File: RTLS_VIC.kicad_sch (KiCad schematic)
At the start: 35 parts, among them J1 Conn_01x02_Pin, SW1 TS-1187A-B-A-B, U1 STM32WLE5CBUx, U3 HXY4612S, U4 TPS63900DSKR, X1 Q24FA20H0021700

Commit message: add notes
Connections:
- net +BATT: no longer C21.1, U4.1 (EN), U4.10 (VIN)
- new net +ESC_5V: C21.1, U4.1 (EN), U4.10 (VIN)
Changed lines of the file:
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@@
 			)
 		)
-		(property "Value" "+BATT"
-			(at 184.15 134.6199 90)
+		(property "Value" "+ESC_5V"
+			(at 186.69 132.08 90)
 			(effects
 				(font
 					(size 1.27 1.27)
 				)
-				(justify left)
 			)
 		)

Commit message: major overhaul
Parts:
- removed C20, C5: 10nF, Capacitor_SMD:C_0402_1005Metric, symbol Device:C
- removed C21, C22, C23: 10uF, Capacitor_SMD:C_0402_1005Metric, symbol Device:C
- removed C25, C26: 12pF, Capacitor_SMD:C_0402_1005Metric, symbol Device:C
- removed C4: 1uF, Capacitor_SMD:C_0402_1005Metric, symbol Device:C
- removed C6, C7, C8: 100nF, Capacitor_SMD:C_0402_1005Metric, symbol Device:C
- removed J1: Conn_01x02_Pin, Connector_PinHeader_2.54mm:PinHeader_1x02_P2.54mm_Vertical, symbol Connector:Conn_01x02_Pin
- removed L6: DFE201612E-2R2M=P2, dfe2016:L0806, symbol dfe2016:DFE201612E-2R2M=P2
- removed R6: 24k, Resistor_SMD:R_0603_1608Metric, symbol Device:R
- removed R7: 100k, Resistor_SMD:R_0603_1608Metric, symbol Device:R
- removed R8: 36k5, Resistor_SMD:R_0603_1608Metric, symbol Device:R
- removed SW1: TS-1187A-B-A-B, ts-1187a-b-a-b:SW-SMD_4P-L5.1-W5.1-P3.70-LS6.5-TL_H1.5, symbol ts-1187a-b-a-b:TS-1187A-B-A-B
- removed U1: STM32WLE5CBUx, Package_DFN_QFN:QFN-48-1EP_7x7mm_P0.5mm_EP5.6x5.6mm, symbol MCU_ST_STM32WL:STM32WLE5CBUx
- removed U3: HXY4612S, hxy4612s:SOP-8_L4.9-W3.9-P1.27-LS6.0-BL, symbol hxy4612s:HXY4612S
- removed U4: TPS63900DSKR, tps63900:WSON-10_L2.5-W2.5-W0.50-TL-EP, symbol tps63900:TPS63900DSKR
- removed X1: Q24FA20H0021700, q24:CRYSTAL-SMD_4P-L2.5-W2.0-BL, symbol q24:Q24FA20H0021700
- added C10, C11: 18pF, Capacitor_SMD:C_0402_1005Metric, symbol Device:C
- added C12, C13, C14, C15, C16, C9: 100nF, Capacitor_SMD:C_0402_1005Metric, symbol Device:C
- added C17: 1uF, Capacitor_SMD:C_0402_1005Metric, symbol Device:C
- added D2, D3: LED, LED_SMD:LED_0603_1608Metric, symbol Device:LED
- added J8: Conn_01x02_Pin, Connector_PinHeader_2.54mm:PinHeader_1x02_P2.54mm_Vertical, symbol Connector:Conn_01x02_Pin
- added L1: DFE201612E-2R2M=P2, lib:L0806, symbol lib:DFE201612E-2R2M=P2
- added R2: 10K, Resistor_SMD:R_0603_1608Metric, symbol Device:R
- added SW1: TS-1187A-B-A-B, lib:SW-SMD_4P-L5.1-W5.1-P3.70-LS6.5-TL_H1.5, symbol lib:TS-1187A-B-A-B
- added U2: TPS63900DSKR, lib:WSON-10_L2.5-W2.5-W0.50-TL-EP, symbol lib:TPS63900DSKR
- added U9: STM32F411RET6, lib:LQFP-64_L10.0-W10.0-P0.50-LS12.0-BL, symbol lib:STM32F411RET6
- added X1: XL2EL89COI-111YLC-26M, lib:CRYSTAL-SMD_4P-L3.2-W2.5-BL_SIT8008BI, symbol lib:XL2EL89COI-111YLC-26M
- C1, C2: value 100nF -> 10uF; LCSC (none) -> C15525
- C3: value 4.7uF -> 10uF; LCSC (none) -> C15525
- R1: value 10K -> 100k; LCSC (none) -> C25803
- R3: value 100K -> 36k5; LCSC (none) -> C23029
- R4: value 7k5 -> 1K
- R5: value 100K -> 1K
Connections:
- net MEAS_EN is gone; now on net GND: R3.1
- net +3V3: now also C12.1, C13.1, C14.1, C15.1, C16.1, C17.1, J8.2 (Pin_2), U2.6 (VOUT), U9.1 (VBAT), U9.19 (VDD), U9.32 (VDD), U9.48 (VDD), U9.64 (VDD); no longer C1.1
- net +ESC_5V: now also C1.1, U2.1 (EN), U2.10 (VIN)
- net GND: now also R1.1, C10.2, C11.1, C12.2, C13.2, C14.2, C15.2, C16.2, C17.2, C9.1, D2.1 (K), D3.1 (K), R2.2, SW1.1 (A), SW1.2 (B), U2.5 (CFG3), U2.8 (GND), U9.12 (VSSA/VREF-), U9.18 (VSS), U9.31 (VSS), U9.47 (VSS), U9.63 (VSS), X1.2 (GND), X1.4 (GND); no longer R1.2, R3.2
- net GPS_RX: now also U9.17 (PA3)
- net GPS_TX: now also U9.16 (PA2)
- net NSS: now also U9.20 (PA4)
- net PWM_1: now also U9.44 (PA11)
- net PWM_2: now also U9.43 (PA10)
- net PWM_3: now also U9.42 (PA9)
- net PWM_4: now also U9.41 (PA8)
- net PWR_SEL: now also R1.2, U2.2 (SEL), U9.33 (PB12)
- net RST: now also C9.2, SW1.3 (C), SW1.4 (D), U9.7 (NRST)
- net SCL: now also U9.58 (PB6)
- net SDA: now also U9.59 (PB7)
- net LED_DEBUG_3: now reaches R4.2
- net LED_DEBUG_3: now also U9.36 (PB15)
- net at R5.1: now also D3.2 (A)
- net +3.3VA renamed VDDA
- net VDDA: now also U9.13 (VDDA/VREF+)
- net +BATT renamed LED_DEBUG_2
- net LED_DEBUG_2: now also U9.35 (PB14)
- net DEBUG_SWCLK renamed SWCLK
- net SWCLK: now also U9.49 (PA14)
- net DEBUG_SWDIO renamed SWDIO
- net SWDIO: now also U9.46 (PA13)
- net LED_DEBUG renamed LED_DEBUG_1
- net LED_DEBUG_1: now also U9.34 (PB13)
- net MEAS_OUT: no longer names the net of R4.1
- net MEAS_OUT: now also D2.2 (A)
- net RX renamed DEBUG_RX
- net DEBUG_RX: now also U9.55 (PB3)
- net TX renamed DEBUG_TX
- net DEBUG_TX: now also U9.50 (PA15)
- new net: R3.2, U2.3 (CFG1)
- new net: L1.2, U2.7 (LX2)
- new net: L1.1, U2.9 (LX1)
- new net BOOT0: J8.1 (Pin_1), R2.1, U9.60 (BOOT0)
- new net SPI_MISO: U9.22 (PA6)
- new net SPI_MOSI: U9.23 (PA7)
- new net SPI_SCK: U9.21 (PA5)
- new net XIN: C11.2, U9.5 (PH0_OSC_IN), X1.1
- new net XOT: C10.1, U9.6 (PH1_OSC_OUT), X1.3
- no-connect marks 10 -> 6
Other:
- removed sheet Radio + Antenna
- moved on the sheet: C24, D1, J2, L7, R10, R11, R9

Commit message: working on placements
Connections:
- net DEBUG_BTN_1: now reaches U9.39 (PC8)
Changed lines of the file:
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@@
+		)
+	)
+	(global_label "DEBUG_BTN_1"
+		(shape input)
+		(at 106.68 95.25 0)
+		(fields_autoplaced yes)
+		(effects
+			(font
+				(size 1.27 1.27)
+			)
+			(justify left)
+		)
+		(property "Intersheetrefs" "${INTERSHEET_REFS}"
+			(at 122.6675 95.25 0)
+			(effects
+				(font
+					(size 1.27 1.27)
+				)
+				(justify left)
+				(hide yes)
+			)
 		)
 	)

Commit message: nearly there
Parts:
- added C4: 4.7uF, Capacitor_SMD:C_0402_1005Metric, symbol Device:C
- added J10, J11, J13: Conn_01x04_Socket, Connector_PinSocket_2.54mm:PinSocket_1x04_P2.54mm_Vertical, symbol Connector:Conn_01x04_Socket
- added J12: Conn_01x02_Pin, Connector_PinHeader_2.54mm:PinHeader_1x02_P2.54mm_Vertical, symbol Connector:Conn_01x02_Pin
- J8: now left out of the parts list
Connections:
- net +3V3: now also J10.1 (Pin_1), J12.2 (Pin_2), J13.1 (Pin_1)
- net GND: now also C4.2, J10.4 (Pin_4), J12.1 (Pin_1), J13.4 (Pin_4)
- net SCL: now also J10.3 (Pin_3)
- net SDA: now also J10.2 (Pin_2)
- net SPI_MISO: now also J11.3 (Pin_3)
- net SPI_MOSI: now also J11.4 (Pin_4)
- net SPI_SCK: now also J11.2 (Pin_2)
- net BMP581_INT: now reaches U9.27 (PB1)
- net LSM6_INT1: now reaches U9.28 (PB2)
- net LSM6_INT2: now reaches U9.29 (PB10)
- net VCAP: now reaches U9.30 (VCAP_1)
- net VCAP: now also C4.1
- net DEBUG_UART6_TX: now reaches U9.37 (PC6)
- net DEBUG_UART6_TX: now also J13.2 (Pin_2)
- net DEBUG_UART6_RX: now reaches U9.38 (PC7)
- net DEBUG_UART6_RX: now also J13.3 (Pin_3)
- net DEBUG_NSS: now reaches U9.45 (PA12)
- net DEBUG_NSS: now also J11.1 (Pin_1)
- no-connect marks 6 -> 23
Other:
- sheet Sensors ports: added BMP581_INT, LSM6_INT1, LSM6_INT2; removed none
- note added: "TODO: Look at the .ioc and include the timing channels for backup PWM channels break out timing channels 2 to pins behind the existing pwm out"
- note added: "Test Connectors"
- moved on the sheet: C1, C2, C3, L1, R1, R3, U2

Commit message: preparing for prod
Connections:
- net DEBUG_NSS: now also U9.24 (PC4); no longer U9.45 (PA12)
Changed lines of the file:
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@@
+	)
+	(no_connect
+		(at 106.68 80.01)
 	)
 	(no_connect
@@
 	(no_connect
 		(at 262.89 36.83)
-	)
-	(no_connect
-		(at 66.04 130.81)
 	)
 	(wire
@@
 		)
 	)
+	(global_label "DEBUG_NSS"
+		(shape input)
+		(at 66.04 130.81 270)
+		(fields_autoplaced yes)
+		(effects
+			(font
+				(size 1.27 1.27)
+			)
+			(justify right)
+		)
+		(property "Intersheetrefs" "${INTERSHEET_REFS}"
+			(at 66.04 144.8018 90)
+			(effects
+				(font
+					(size 1.27 1.27)
+				)
+				(justify right)
+				(hide yes)
+			)
+		)
+	)
 	(global_label "LSM6_INT1"
 		(shape output)
@@
 				(hide yes)
 			)
-		)
-	)
-	(global_label "DEBUG_NSS"
-		(shape input)
-		(at 106.68 80.01 0)
-		(fields_autoplaced yes)
-		(effects
-			(font
-				(size 1.27 1.27)
-			)
-			(justify left)
-		)
-		(property "Intersheetrefs" "${INTERSHEET_REFS}"
-			(at 120.6718 80.01 0)
-			(effects
-				(font
-					(size 1.27 1.27)
-				)
-				(justify left)
-				(hide yes)
-			)

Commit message: prod1
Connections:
- net BMP581_INT: no longer names the net of U9.27 (PB1)
- no-connect marks 23 -> 24
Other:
- sheet Sensors ports: added none; removed BMP581_INT
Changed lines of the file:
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@@
 	)
 	(no_connect
+		(at 73.66 130.81)
+	)
+	(no_connect
 		(at 73.66 52.07)
 	)
@@
 		)
 	)
-	(global_label "BMP581_INT"
-		(shape output)
-		(at 73.66 130.81 270)
-		(effects
-			(font
-				(size 1.27 1.27)
-			)
-			(justify right)
-		)
-		(property "Intersheetrefs" "${INTERSHEET_REFS}"
-			(at 73.66 130.81 0)
-			(effects
-				(font
-					(size 1.27 1.27)
-				)
-				(hide yes)
-			)
-		)
-	)
 	(global_label "LED_DEBUG_3"
 		(shape input)
@@
 		)
 	)
-	(global_label "BMP581_INT"
-		(shape output)
-		(at 143.51 177.8 180)
-		(effects
-			(font
-				(size 1.27 1.27)
-			)
-			(justify right)
-		)
-		(property "Intersheetrefs" "${INTERSHEET_REFS}"
-			(at 143.51 177.8 0)
-			(effects
-				(font
-					(size 1.27 1.27)
-				)
-				(hide yes)
-			)
-		)
-	)
 	(symbol
 		(lib_id "power:+3V3")
@@
 			(effects
 				(font
-					(size 1.27 1.27)
-				)
-				(justify left)
-			)
-		)
-		(pin "BMP581_INT" output
-			(at 143.51 177.8 180)
-			(effects
-				(font

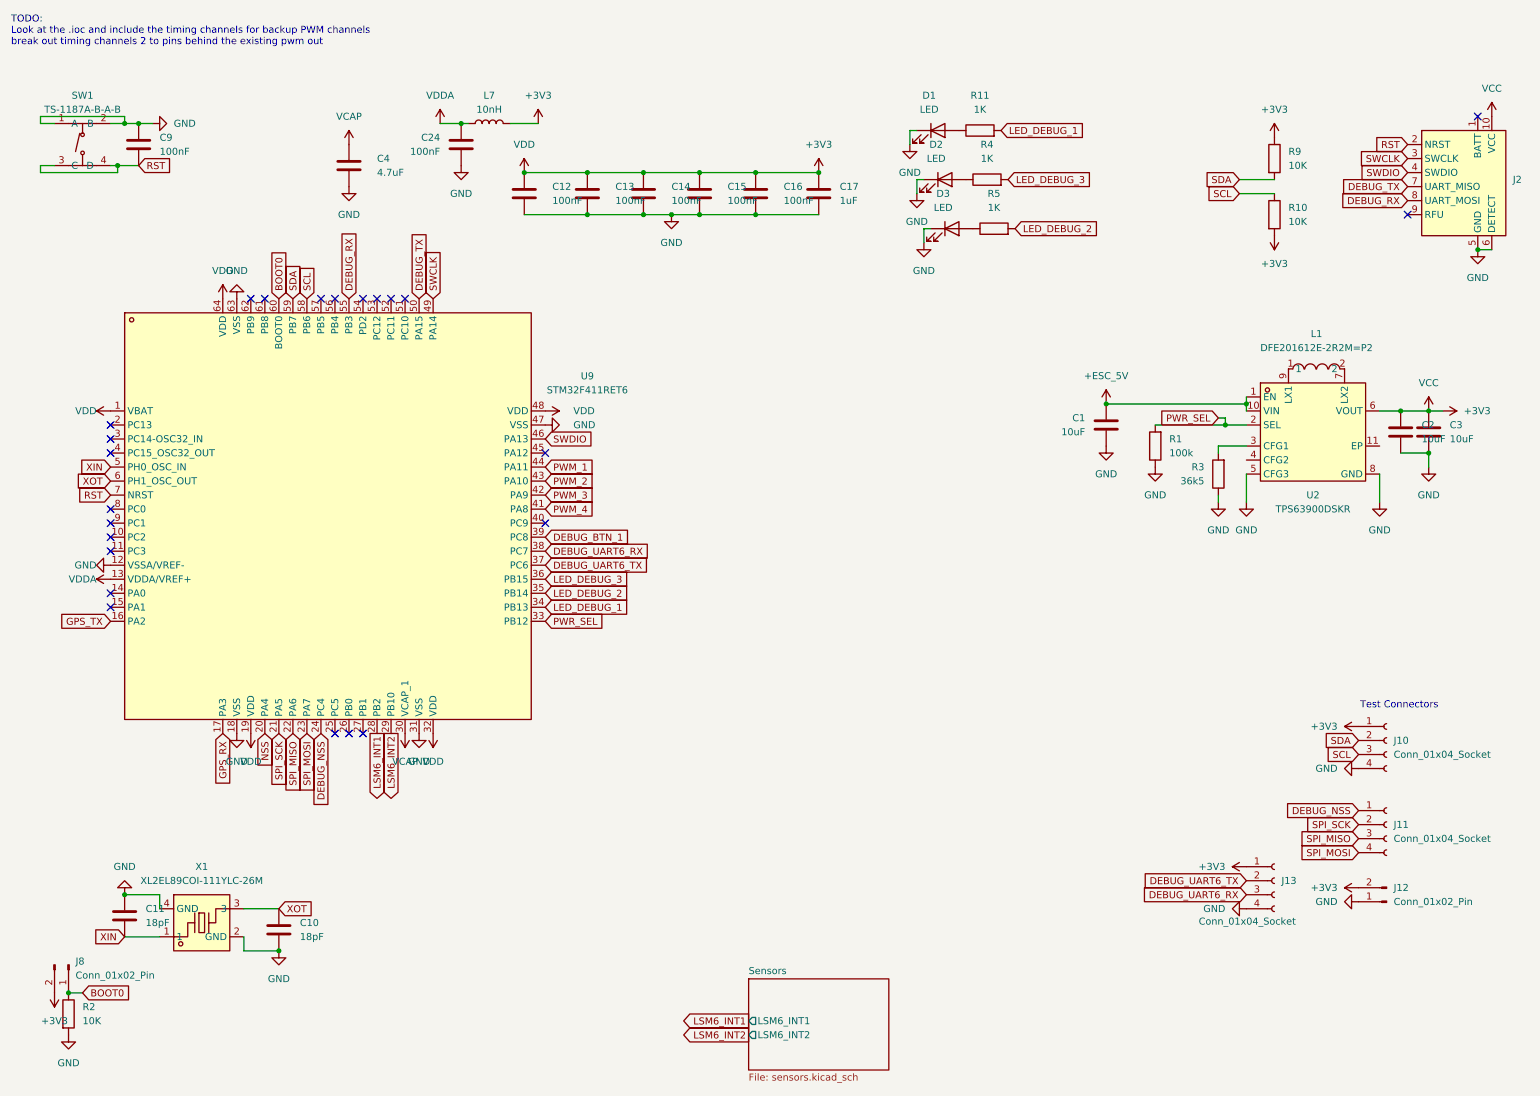
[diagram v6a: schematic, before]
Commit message: forgot to do timing channel 2
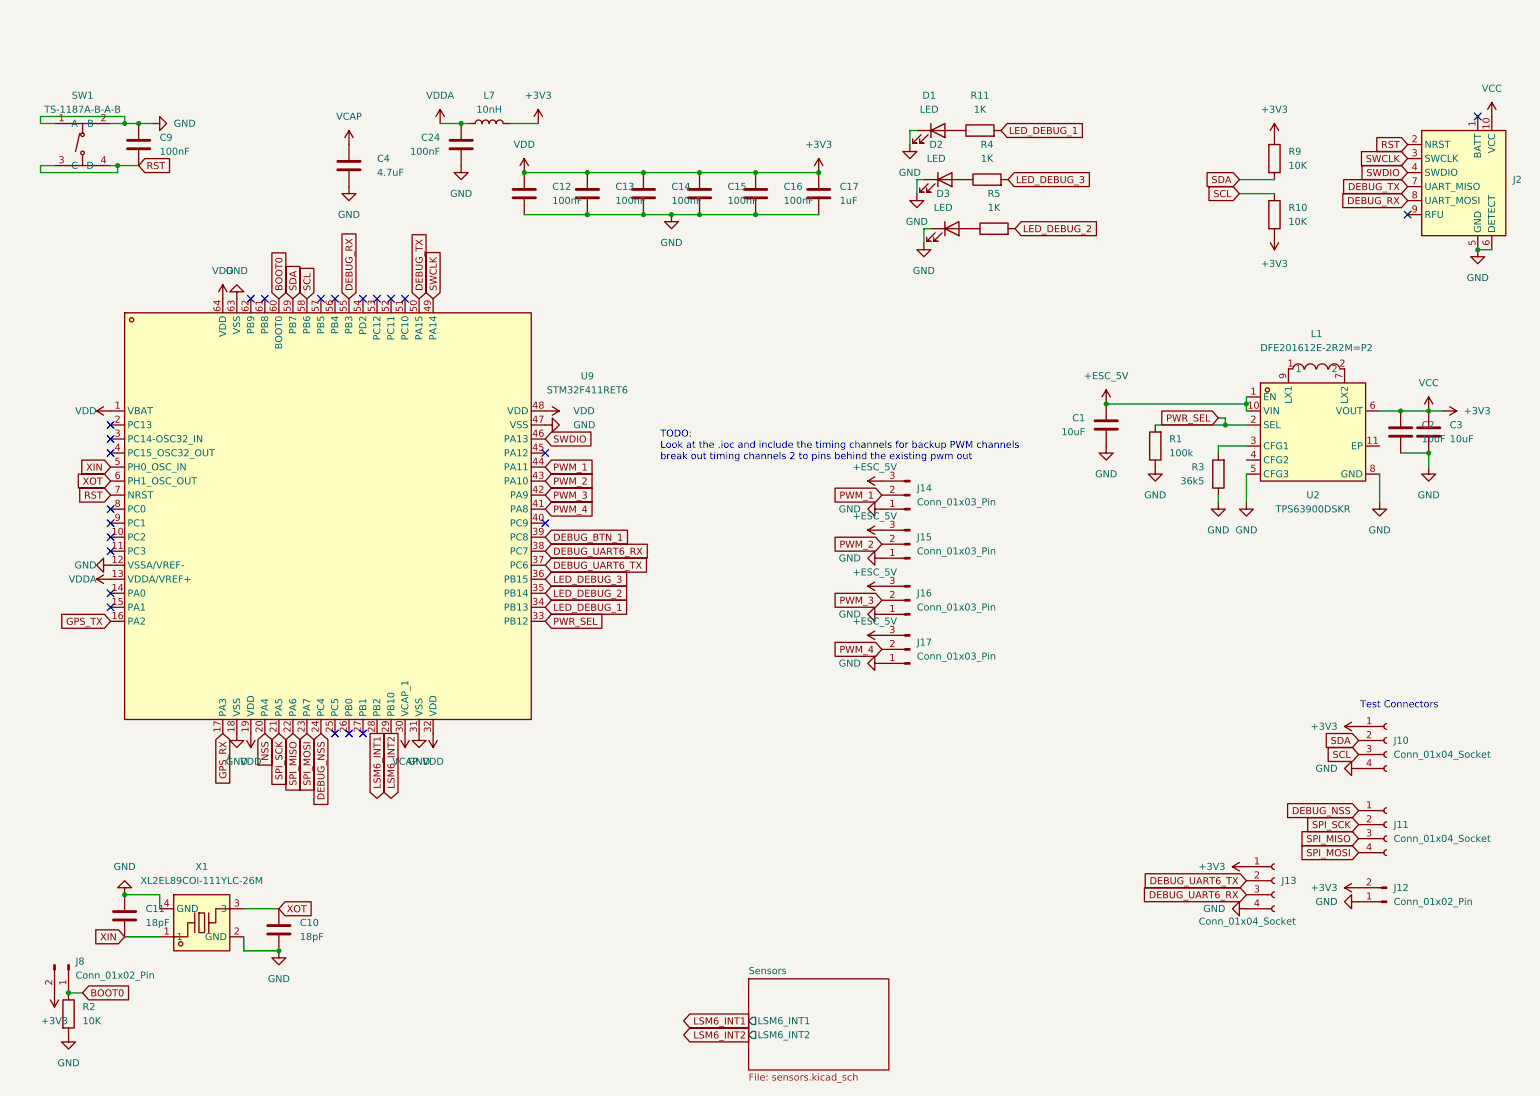
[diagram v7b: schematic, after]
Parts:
- added J14, J15, J16, J17: Conn_01x03_Pin, Connector_PinHeader_2.54mm:PinHeader_1x03_P2.54mm_Vertical, symbol Connector:Conn_01x03_Pin
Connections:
- net +ESC_5V: now also J14.3 (Pin_3), J15.3 (Pin_3), J16.3 (Pin_3), J17.3 (Pin_3)
- net GND: now also J14.1 (Pin_1), J15.1 (Pin_1), J16.1 (Pin_1), J17.1 (Pin_1)
- net PWM_1: now also J14.2 (Pin_2)
- net PWM_2: now also J15.2 (Pin_2)
- net PWM_3: now also J16.2 (Pin_2)
- net PWM_4: now also J17.2 (Pin_2)

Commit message: sponsor and timing
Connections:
- net PWM_1: no longer J14.2 (Pin_2)
- net PWM_2: no longer J15.2 (Pin_2)
- net PWM_3: no longer J16.2 (Pin_2)
- net PWM_4: no longer J17.2 (Pin_2)
- net PWM_CH2_3: now reaches U9.26 (PB0)
- net PWM_CH2_3: now also J16.2 (Pin_2)
- net PWM_CH2_4: now reaches U9.27 (PB1)
- net PWM_CH2_4: now also J17.2 (Pin_2)
- net PWM_CH2_1: now reaches U9.56 (PB4)
- net PWM_CH2_1: now also J14.2 (Pin_2)
- net PWM_CH2_2: now reaches U9.57 (PB5)
- net PWM_CH2_2: now also J15.2 (Pin_2)
- no-connect marks 24 -> 20
